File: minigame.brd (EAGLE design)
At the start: 97.5 x 41.9 mm, 49 parts, among them J1 AVR_SPI_PRG_6PTH, Q1 MMBT2222A, U1 MCP73831, U2 MIC5219 3.3V, Y1 8MHz

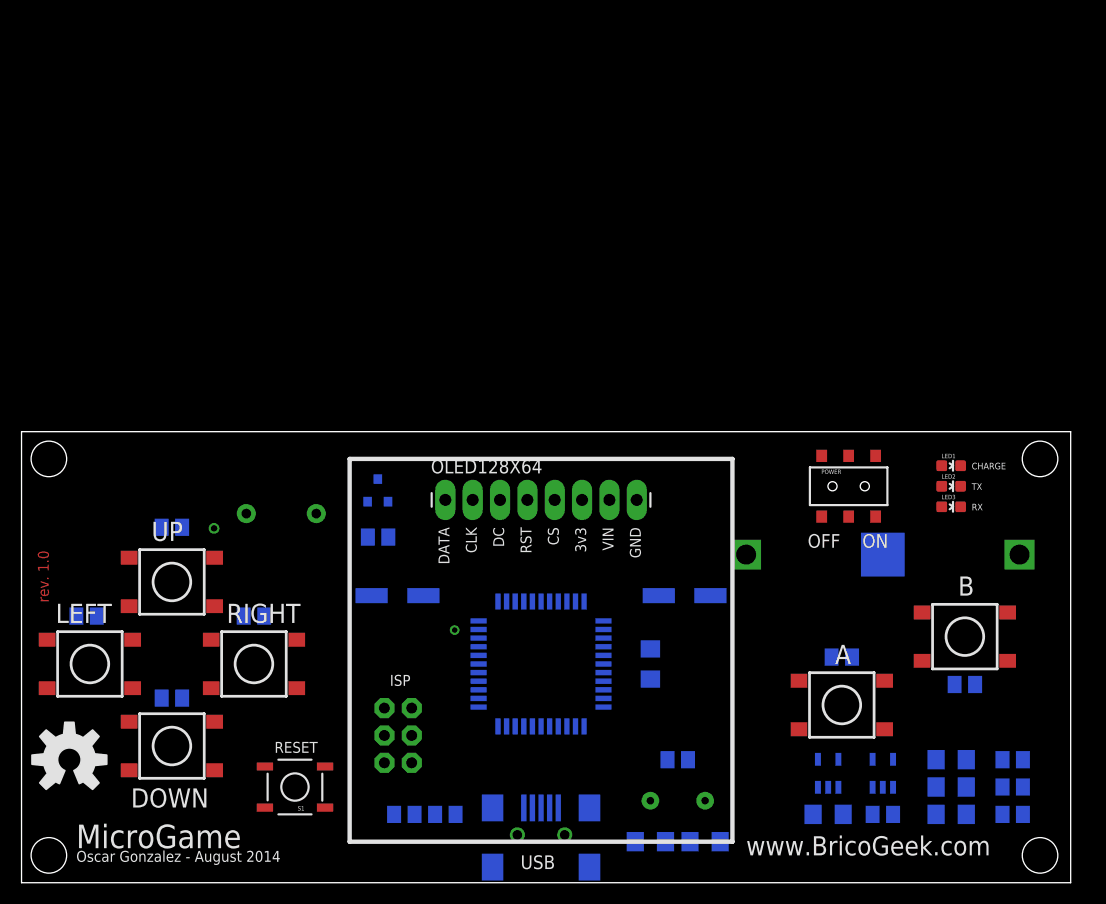
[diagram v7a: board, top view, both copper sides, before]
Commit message: Voltage regulator removed Preliminary Routing test
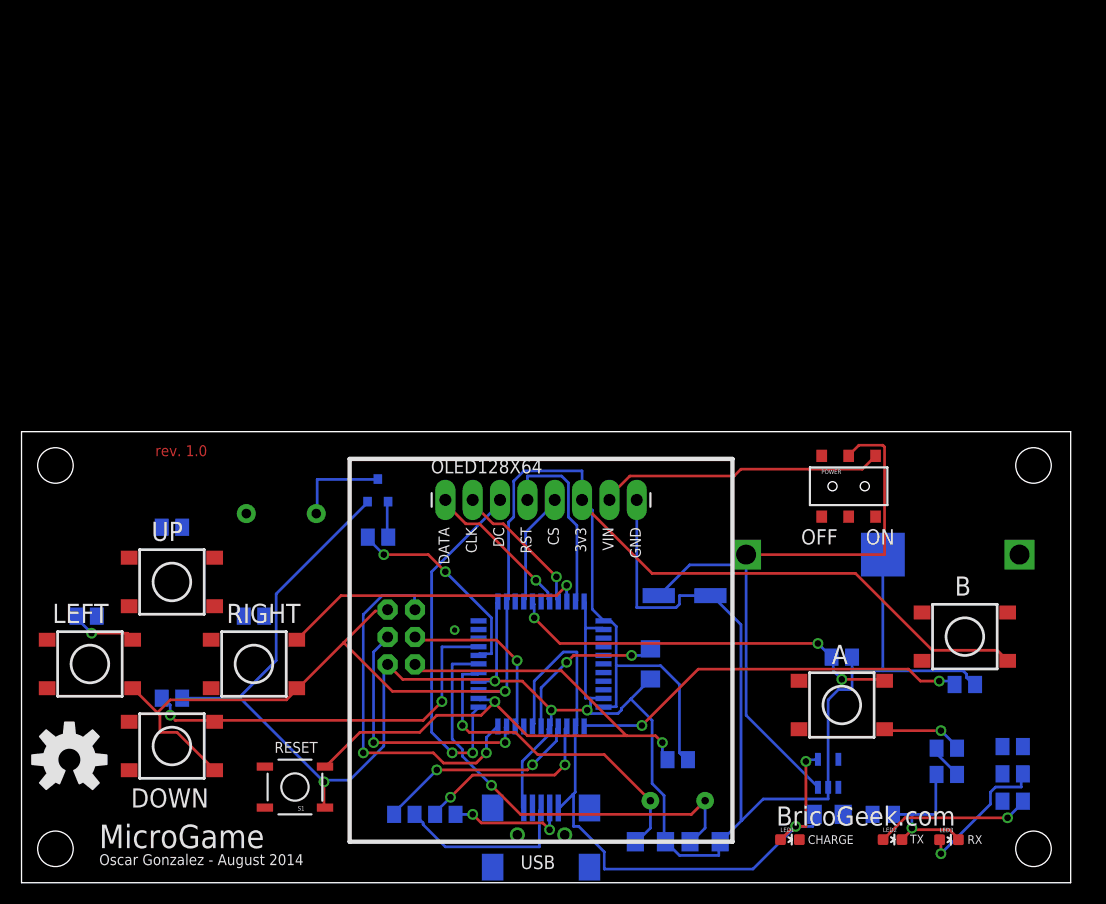
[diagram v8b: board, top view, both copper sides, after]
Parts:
- removed C6: 10uF, SparkFun-Capacitors:PANASONIC_D
- removed C7: 470pF, SparkFun-Passives:1206
- removed C8: 1uF, SparkFun-Passives:1206
- removed C9: 0.1uF, SparkFun-Passives:1206
- removed J1: AVR_SPI_PRG_6PTH, SparkFun-Connectors:2X3
- removed U2: MIC5219 3.3V, SparkFun-PowerIC:SOT23-5
- added ICSP: AVR_SPI_PRG_6PTH, SparkFun-Connectors:2X3
- added R15, R16: 10k, rcl:M0805
- moved LED1 37.8 mm to (71.4, 4.01)
- moved LED2 33.3 mm to (80.9, 4.01)
- moved LED3 30.9 mm to (86.2, 3.99)
- moved R11 1.22 mm to (92.1, 12.6)
- moved R13 1.22 mm to (92.1, 7.57)
- moved R14 1.22 mm to (92.1, 10.1)
- moved U$6 0.86 mm to (94.0, 38.8)
- moved U$2 0.86 mm to (3.15, 38.8)
- moved U$5 0.86 mm to (94.0, 3.15)
- moved U$4 0.86 mm to (3.15, 3.15)
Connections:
- removed net N$10: POWER.3, U2.1, U2.3
- removed net N$8: C7.2, U2.4
- new net POWER: OLED128X64.7, POWER.3
- net 3.3V: now also ICSP.2, OLED128X64.6, R15.1; no longer C6.+, C8.2, C9.2, J1.2, OLED128X64.7, U2.5
- net GND: now also ICSP.6, R16.2; no longer C6.-, C7.1, C8.1, C9.1, J1.6, U2.2
- net MISO: now also ICSP.1; no longer J1.1
- net MOSI: now also ICSP.4; no longer J1.4
- net RST: now also ICSP.5; no longer J1.5
- net SCK: now also ICSP.3; no longer J1.3
- net VBAT: now also R15.2, R16.1
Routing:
- net GND: track 0.00 -> 243.9 mm, vias 0 -> 5
- net 3.3V: track 0.00 -> 175.5 mm, vias 0 -> 2
- net VBUS: track 0.00 -> 65.4 mm, vias 0 -> 2
- net VBAT: track 0.00 -> 63.6 mm
- net RST: track 0.00 -> 61.4 mm, vias 0 -> 2
- net N$1: track 0.00 -> 41.2 mm, vias 0 -> 1
- net B: track 0.00 -> 37.4 mm, vias 0 -> 2
- net A: track 0.00 -> 37.4 mm, vias 0 -> 3
- net DOWN: track 0.00 -> 36.8 mm, vias 0 -> 2
- net MISO: track 0.00 -> 34.8 mm, vias 0 -> 2
- net OLED_DC: track 0.00 -> 33.3 mm, vias 0 -> 2
- net N$2: track 0.00 -> 31.2 mm, vias 0 -> 1
- net RIGHT: track 0.00 -> 28.7 mm, vias 0 -> 1
- net POWER: track 0.00 -> 26.6 mm
- net MOSI: track 0.00 -> 24.1 mm, vias 0 -> 2
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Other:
- board text added: "ATMega32U4"
- board text added: "BricoGeek.com"
- board text removed: "ISP"
- board text removed: "www.BricoGeek.com"
